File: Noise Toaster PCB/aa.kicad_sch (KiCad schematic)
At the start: 17 parts, among them J1 Line Out, U4 LM386, X12 Conn_01x01_Pin

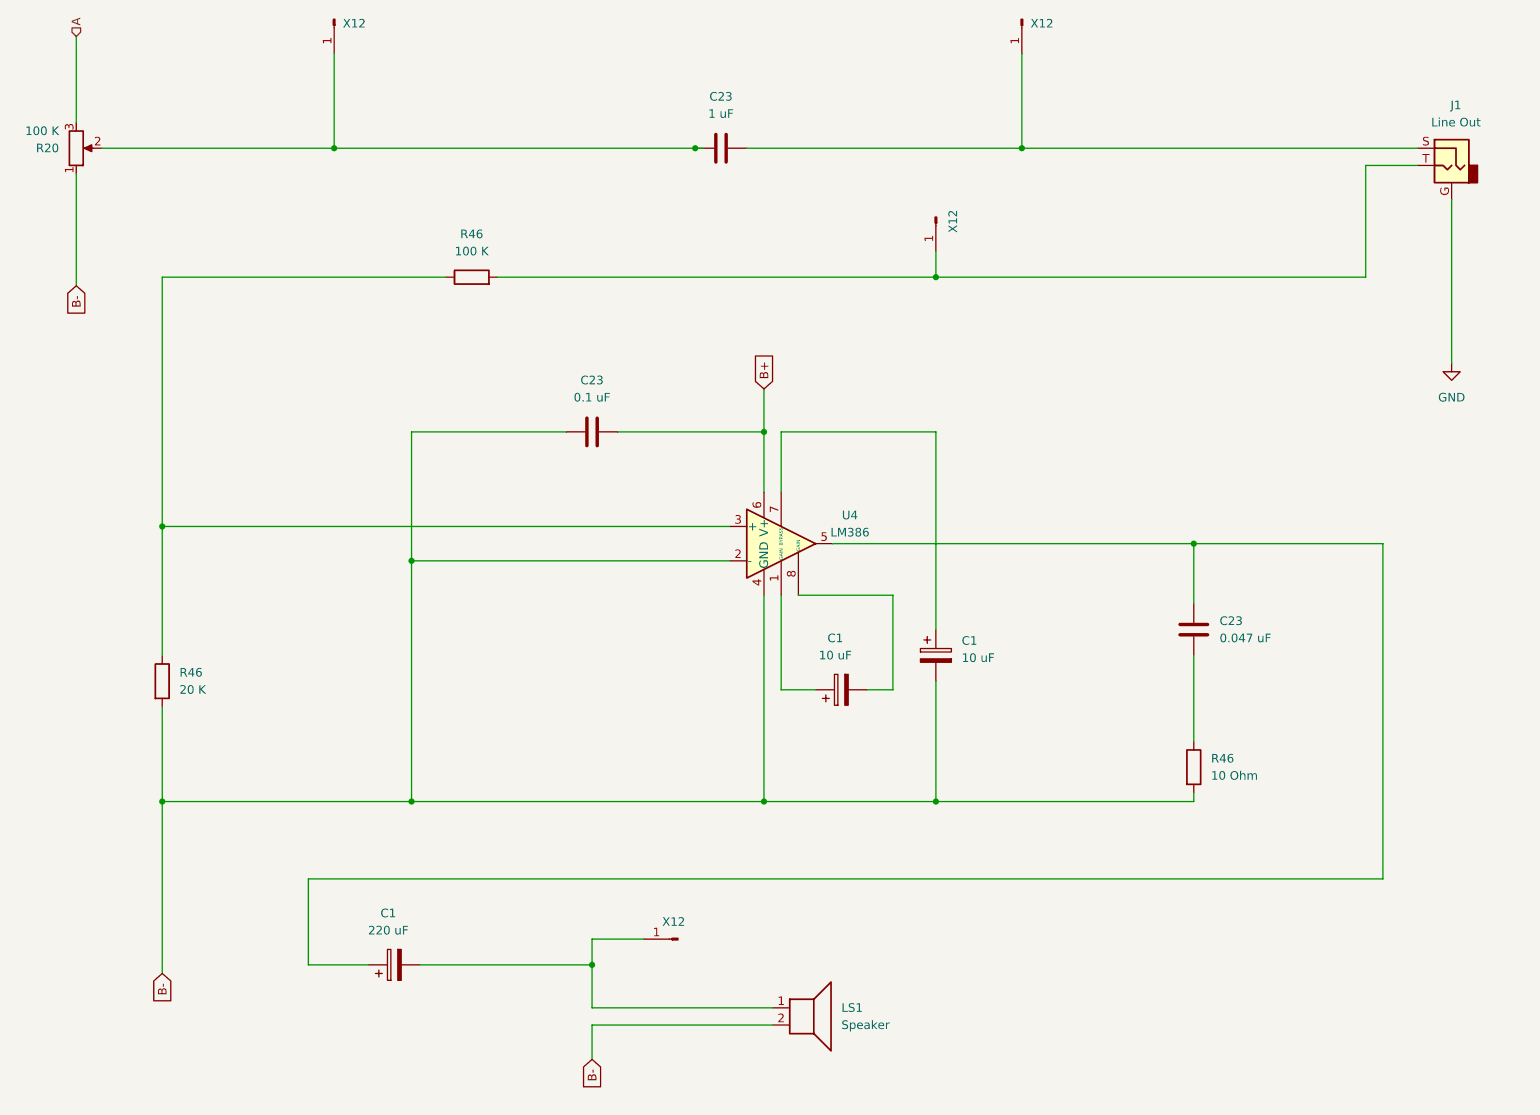
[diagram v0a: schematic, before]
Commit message: updated schematics
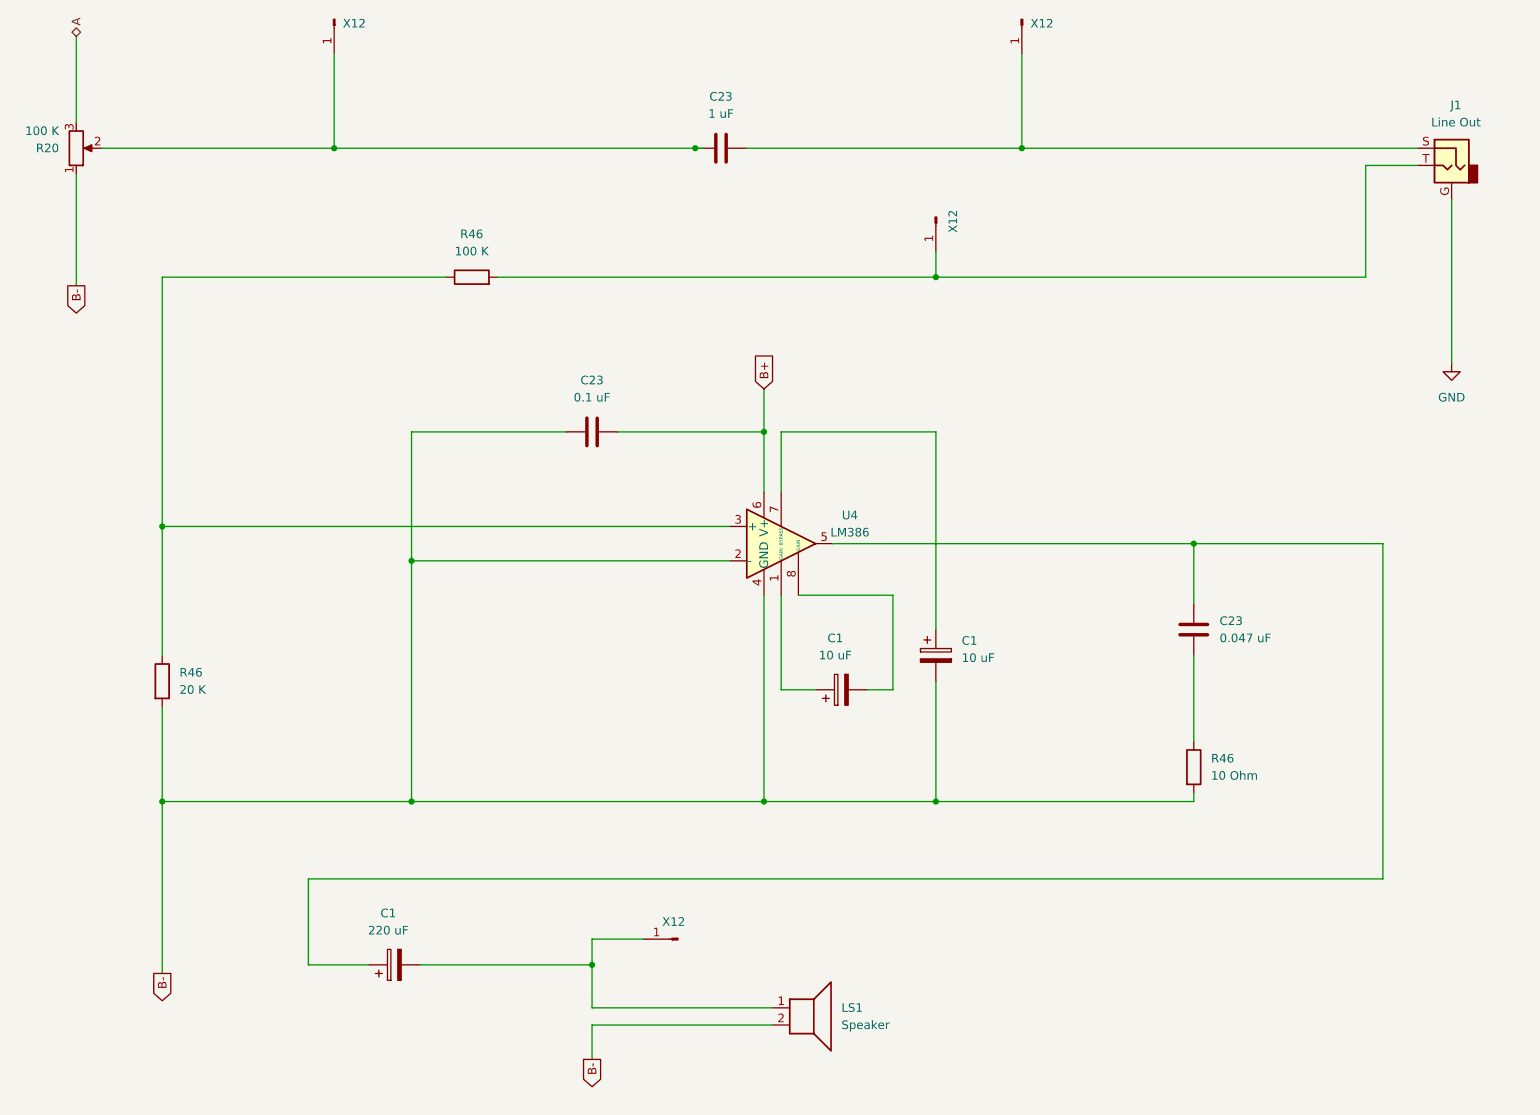
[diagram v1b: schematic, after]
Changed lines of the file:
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@@
     (stroke (width 0) (type default))
   )
-  (global_label "B-" (shape input) (at 114.3 179.07 270) (fields_autoplaced)
+  (global_label "B-" (shape output) (at 114.3 179.07 270) (fields_autoplaced)
     (effects (font (size 1.27 1.27)) (justify right))
     (property "Intersheetrefs" "${INTERSHEET_REFS}" (at 114.3 184.8976 90)
@@
     )
   )
-  (global_label "B-" (shape input) (at 38.1 64.77 270) (fields_autoplaced)
+  (global_label "B-" (shape output) (at 38.1 64.77 270) (fields_autoplaced)
     (effects (font (size 1.27 1.27)) (justify right))
     (property "Intersheetrefs" "${INTERSHEET_REFS}" (at 38.1 70.5976 90)
@@
     )
   )
-  (global_label "B-" (shape input) (at 50.8 166.37 270) (fields_autoplaced)
+  (global_label "B-" (shape output) (at 50.8 166.37 270) (fields_autoplaced)
     (effects (font (size 1.27 1.27)) (justify right))
     (property "Intersheetrefs" "${INTERSHEET_REFS}" (at 50.8 172.1976 90)
@@
     )
   )
-  (hierarchical_label "A" (shape input) (at 38.1 27.94 90) (fields_autoplaced)
+  (hierarchical_label "A" (shape bidirectional) (at 38.1 27.94 90) (fields_autoplaced)
     (effects (font (size 1.27 1.27)) (justify left))
   )
@@
     (instances
       (project "Noise Toaster PCB"
-        (path "/7be3f398-d902-4566-9ee4-0bff072cd47e/9c6b1f0b-dddb-43c5-83ba-4fcd1cf28662"
-          (reference "C23") (unit 1)
-        )
         (path "/7be3f398-d902-4566-9ee4-0bff072cd47e/8b7babf3-8af2-4de0-abdc-510e7f40fd33"
           (reference "C24") (unit 1)
@@
     (instances
       (project "Noise Toaster PCB"
-        (path "/7be3f398-d902-4566-9ee4-0bff072cd47e/9c6b1f0b-dddb-43c5-83ba-4fcd1cf28662"
-          (reference "C23") (unit 1)
-        )
         (path "/7be3f398-d902-4566-9ee4-0bff072cd47e/8b7babf3-8af2-4de0-abdc-510e7f40fd33"
           (reference "C20") (unit 1)
@@
     (instances
       (project "Noise Toaster PCB"
-        (path "/7be3f398-d902-4566-9ee4-0bff072cd47e/9c6b1f0b-dddb-43c5-83ba-4fcd1cf28662"
-          (reference "#PWR01") (unit 1)
-        )
         (path "/7be3f398-d902-4566-9ee4-0bff072cd47e/a3e9deee-1b9d-4545-a3c9-71b211642b5b"
           (reference "#PWR04") (unit 1)
@@
     (instances
       (project "Noise Toaster PCB"
-        (path "/7be3f398-d902-4566-9ee4-0bff072cd47e/9c6b1f0b-dddb-43c5-83ba-4fcd1cf28662"
-          (reference "C23") (unit 1)
-        )
         (path "/7be3f398-d902-4566-9ee4-0bff072cd47e/8b7babf3-8af2-4de0-abdc-510e7f40fd33"
           (reference "C21") (unit 1)

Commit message: refactored the schematic
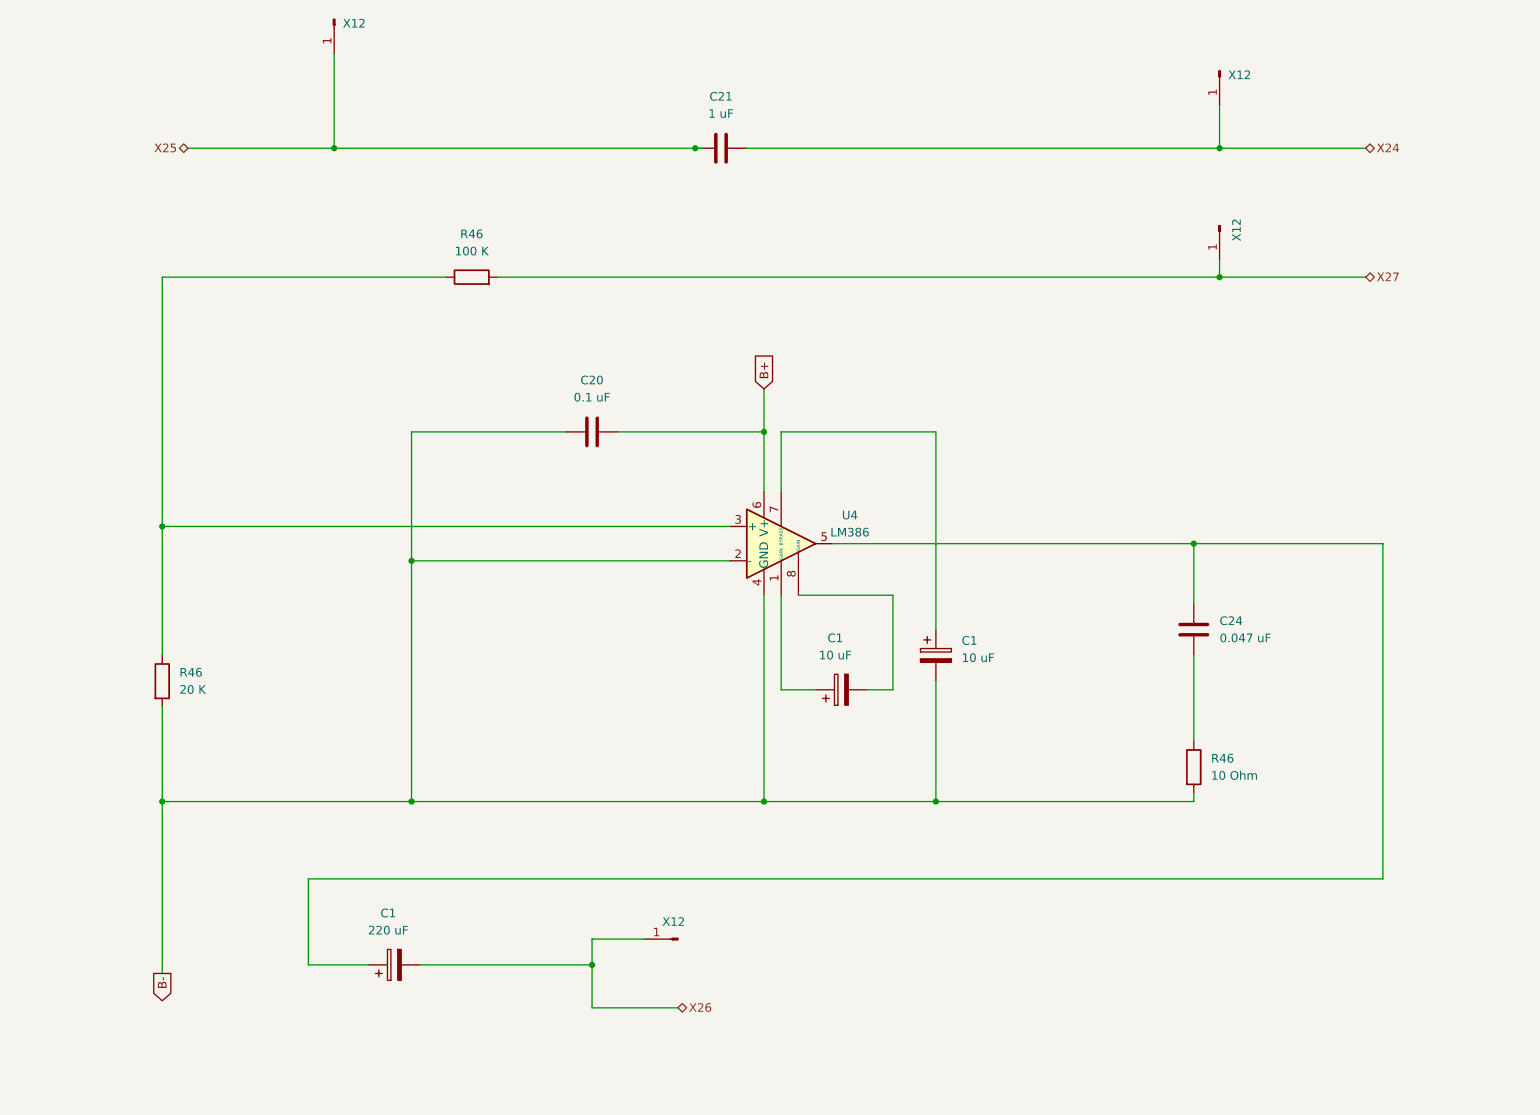
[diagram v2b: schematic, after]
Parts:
- removed J1: Line Out, symbol Connector_Audio:AudioJack2_Ground
- removed LS1: Speaker, symbol Device:Speaker
- removed R20: 100 K, symbol Device:R_Potentiometer
- renumbered C23 to C20, C23 to C21, C23 to C24
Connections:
- net X24: now reaches C21.2, X12.1 (Pin_1)
- net X27: now reaches R46.2, X12.1 (Pin_1)
- net X26: now reaches C1.2, X12.1 (Pin_1)
- net X25: now reaches C21.1, X12.1 (Pin_1)
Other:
- moved on the sheet: X12

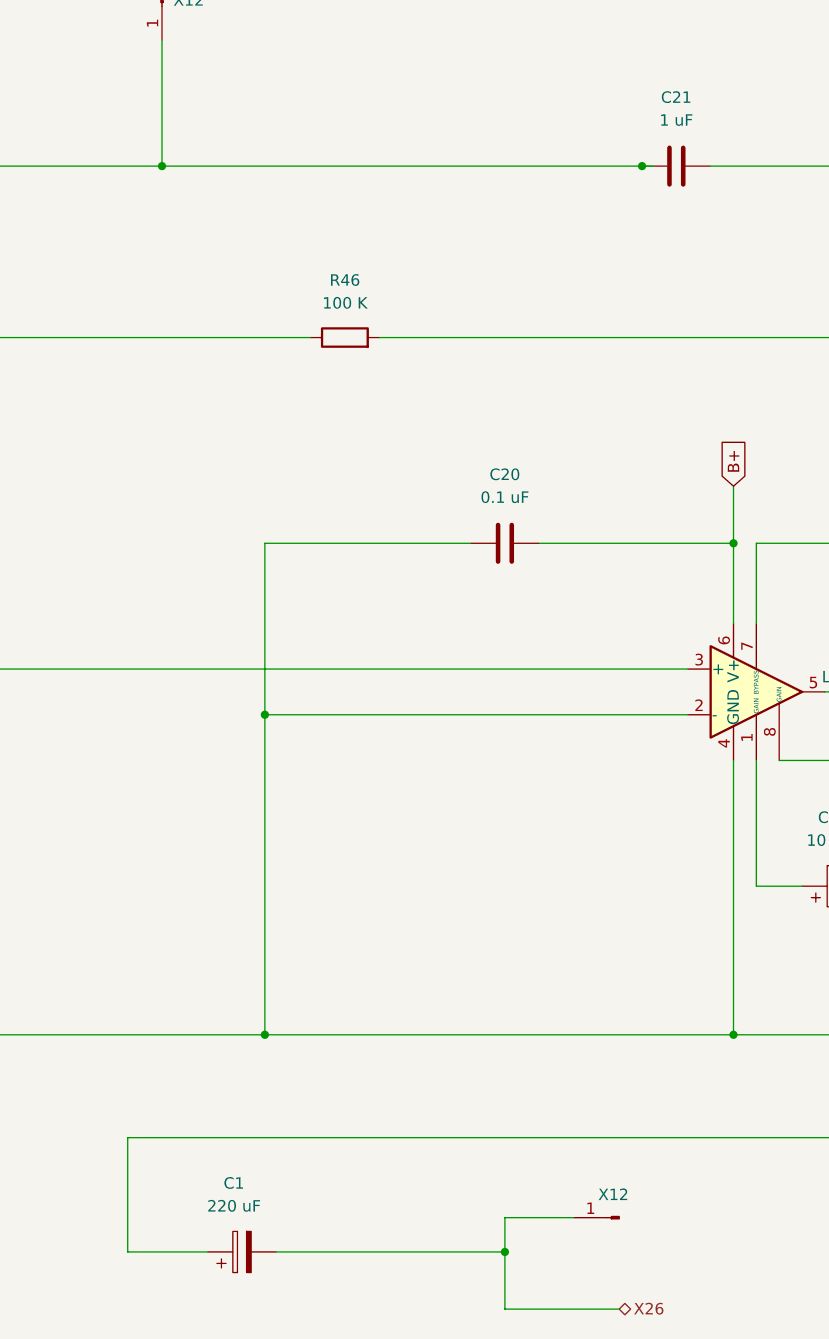
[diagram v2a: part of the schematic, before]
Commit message: refactored schematics and added front panel
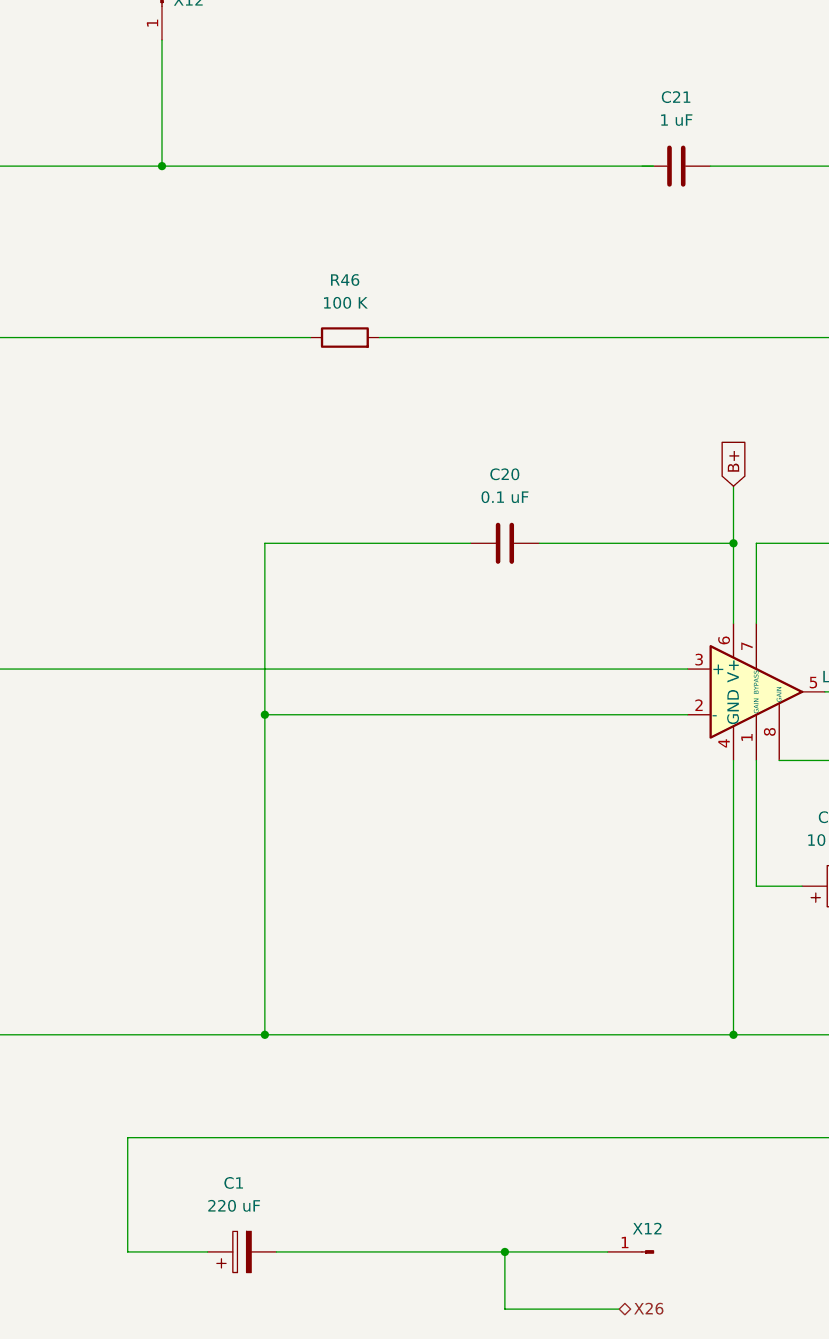
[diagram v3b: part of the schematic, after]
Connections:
- net X25: no longer C21.1
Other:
- moved on the sheet: X12
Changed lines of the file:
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@@
   (junction (at 203.2 102.87) (diameter 0) (color 0 0 0 0)
   )
-  (junction (at 129.54 44.45) (diameter 0) (color 0 0 0 0)
-  )
   (junction (at 207.01 44.45) (diameter 0) (color 0 0 0 0)
   )
@@
     (stroke (width 0) (type default))
   )
-  (wire (pts (xy 114.3 161.29) (xy 114.3 165.1))
-    (stroke (width 0) (type default))
-  )
   (wire (pts (xy 134.62 105.41) (xy 87.63 105.41))
     (stroke (width 0) (type default))
@@
   )
   (wire (pts (xy 87.63 140.97) (xy 50.8 140.97))
-    (stroke (width 0) (type default))
-  )
-  (wire (pts (xy 76.2 44.45) (xy 129.54 44.45))
     (stroke (width 0) (type default))
   )
@@
     (stroke (width 0) (type default))
   )
-  (wire (pts (xy 121.92 161.29) (xy 114.3 161.29))
+  (wire (pts (xy 125.73 165.1) (xy 114.3 165.1))
     (stroke (width 0) (type default))
   )
@@
     (stroke (width 0) (type default))
   )
-  (wire (pts (xy 129.54 44.45) (xy 130.81 44.45))
+  (wire (pts (xy 76.2 44.45) (xy 130.81 44.45))
     (stroke (width 0) (type default))
   )
@@
   (hierarchical_label "X25" (shape bidirectional) (at 54.61 44.45 180)
     (effects (font (size 1.27 1.27)) (justify right))
-    (property "Name " "A" (at 50.8 46.99 0)
-      (effects (font (size 1.27 1.27) italic) (justify right))
-    )
-  )
-  (symbol (lib_id "Connector:Conn_01x01_Pin") (at 127 161.29 180) (unit 1)
+    (property "Name " "" (at 50.8 46.99 0)
+      (effects (font (size 1.27 1.27) italic) (justify right) hide)
+    )
+  )
+  (symbol (lib_id "Connector:Conn_01x01_Pin") (at 130.81 165.1 180) (unit 1)
     (in_bom yes) (on_board yes) (dnp no)
-    (property "Reference" "X12" (at 126.365 158.75 0)
-      (effects (font (size 1.27 1.27)))
-    )
-    (property "Value" "Conn_01x01_Pin" (at 125.095 162.56 90)
+    (property "Reference" "X12" (at 130.175 162.56 0)
+      (effects (font (size 1.27 1.27)))
+    )
+    (property "Value" "Conn_01x01_Pin" (at 128.905 166.37 90)
       (effects (font (size 1.27 1.27)) (justify left) hide)
     )
-    (property "Footprint" "" (at 127 161.29 0)
-      (effects (font (size 1.27 1.27)) hide)
-    )
-    (property "Datasheet" "~" (at 127 161.29 0)
+    (property "Footprint" "" (at 130.81 165.1 0)
+      (effects (font (size 1.27 1.27)) hide)
+    )
+    (property "Datasheet" "~" (at 130.81 165.1 0)
       (effects (font (size 1.27 1.27)) hide)
     )
@@
         )
         (path "/7be3f398-d902-4566-9ee4-0bff072cd47e/8b7babf3-8af2-4de0-abdc-510e7f40fd33"
-          (reference "R66") (unit 1)
-        )
-      )
+          (reference "R68") (unit 1)
+        )
+      )
